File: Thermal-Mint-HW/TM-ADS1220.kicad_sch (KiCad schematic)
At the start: 19 parts, among them U1 ADS1220-VQFN

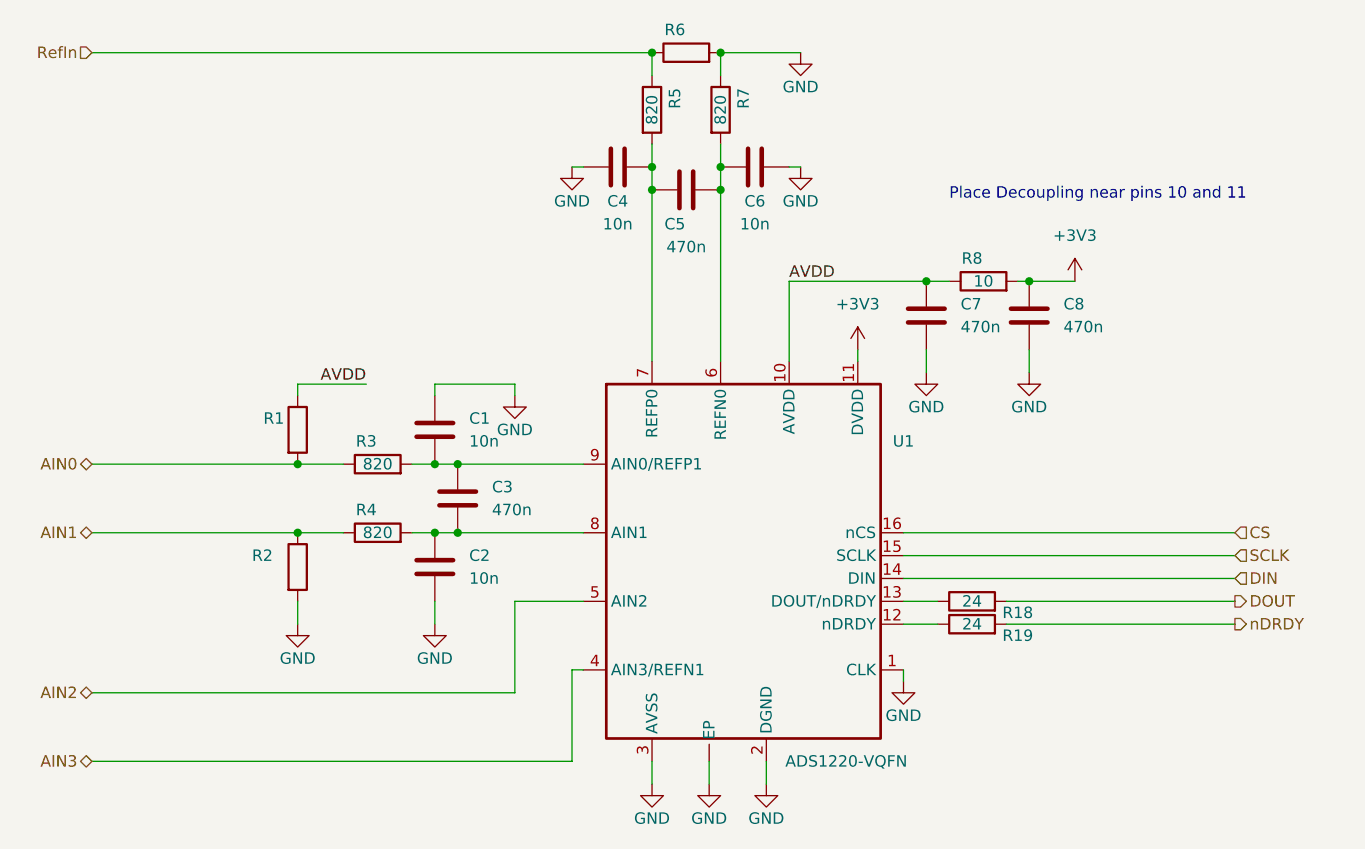
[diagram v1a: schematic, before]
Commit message: Cleanup of Rev1 schematics for review
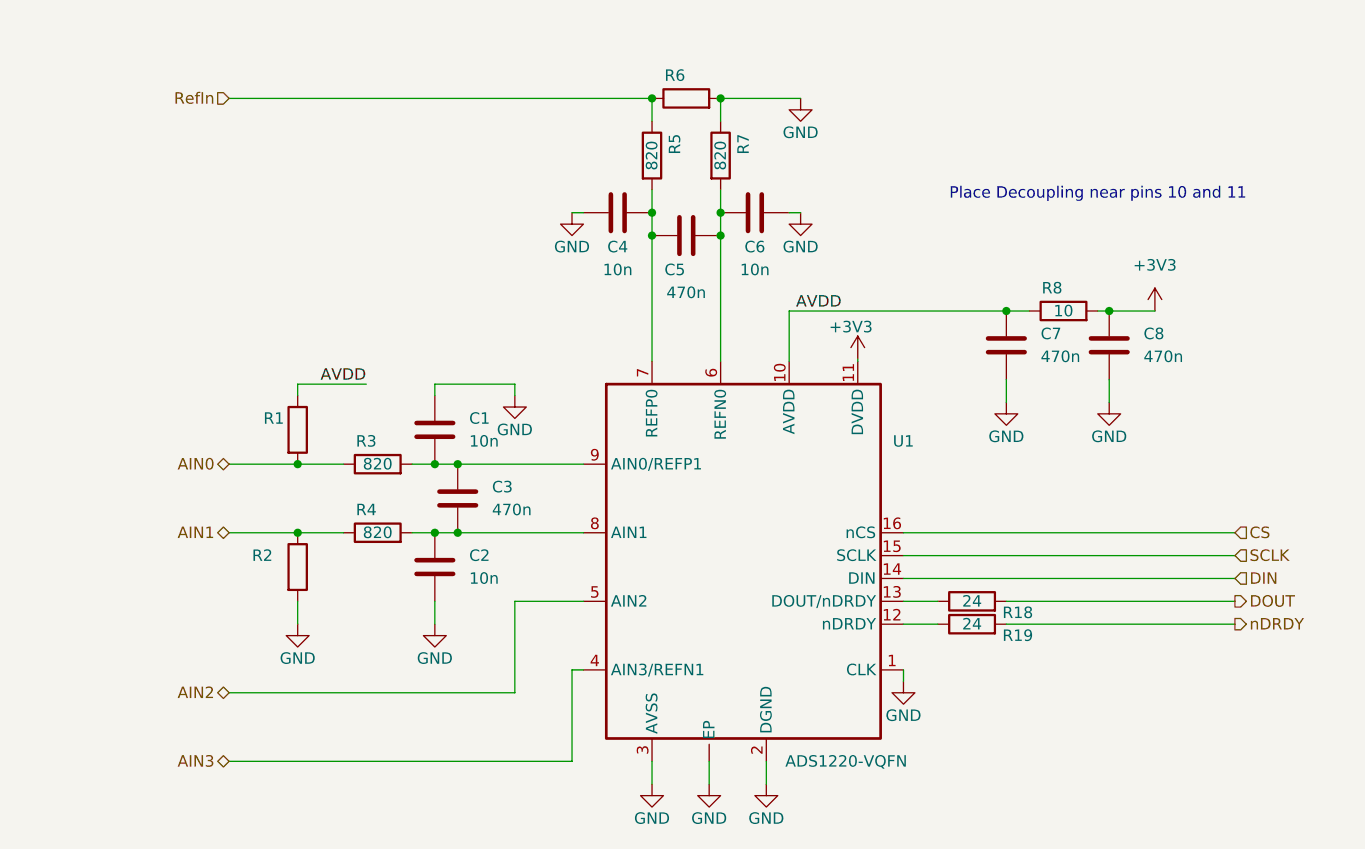
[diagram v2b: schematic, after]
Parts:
- R1, R2: value 10k -> (none); footprint Resistor_SMD:R_0603_1608Metric_Pad0.98x0.95mm_HandSolder -> (none)
- R6: value 1.65k -> (none); footprint Resistor_SMD:R_0603_1608Metric_Pad0.98x0.95mm_HandSolder -> (none)
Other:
- moved on the sheet: C4, C5, C6, C7, C8, R5, R6, R7, R8

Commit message: Temporary commit before changing processor from C3 to s2
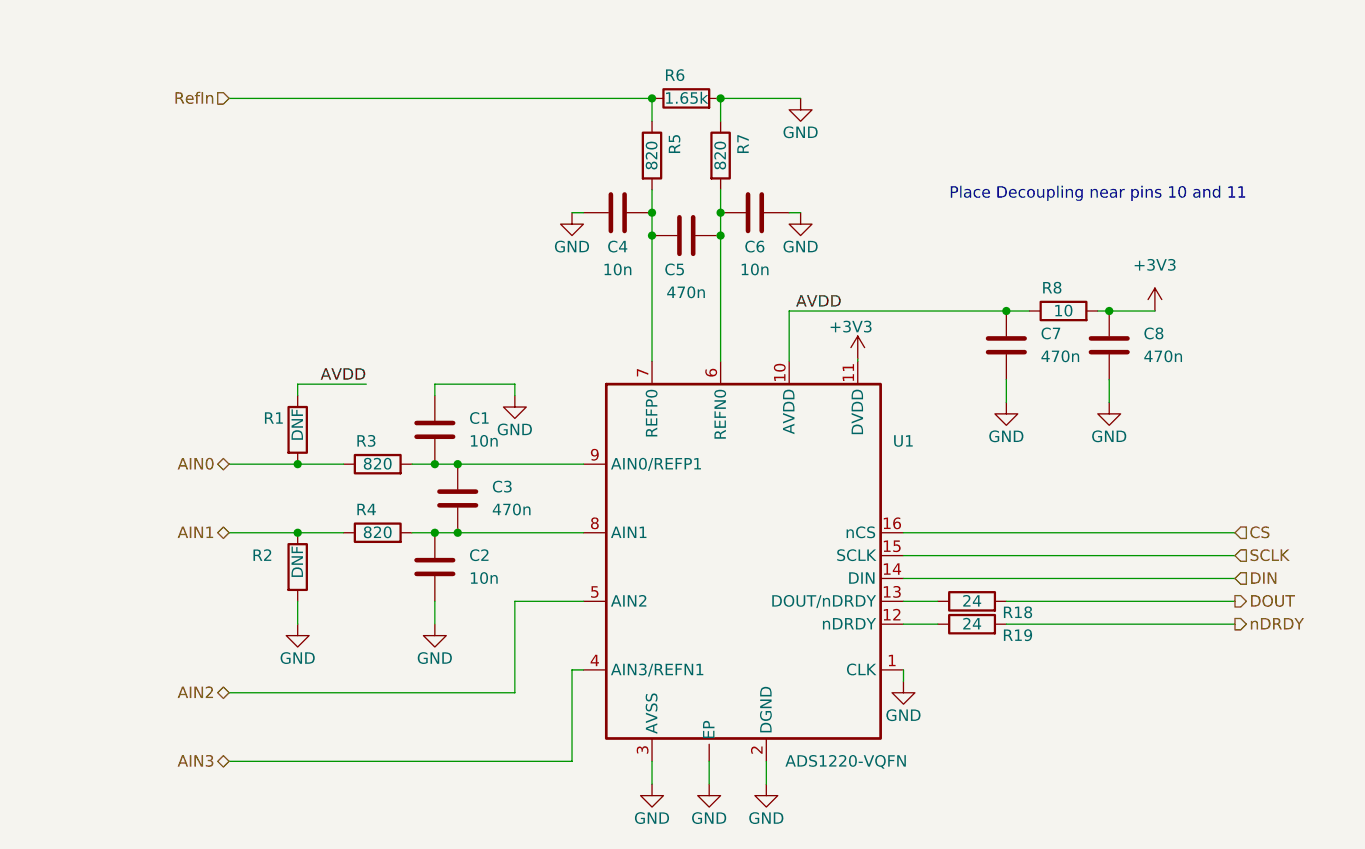
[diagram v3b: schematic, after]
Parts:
- R1, R2: value (none) -> DNF; footprint (none) -> Resistor_SMD:R_0603_1608Metric_Pad0.98x0.95mm_HandSolder
- R6: value (none) -> 1.65k; footprint (none) -> Resistor_SMD:R_0603_1608Metric_Pad0.98x0.95mm_HandSolder

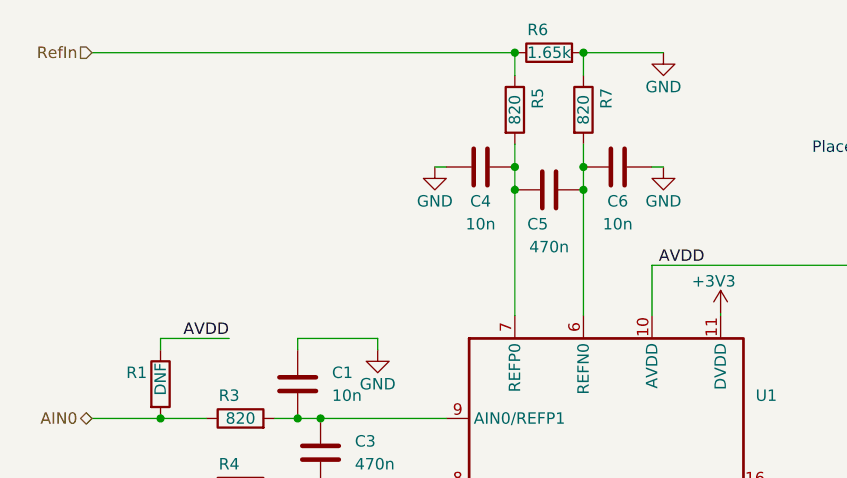
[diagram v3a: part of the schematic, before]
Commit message: Schematic update to ESP32-S2
Updated schematic from ESP32-C3 to the S2 chips with more pins, allowed the removal of the GPO expander and CS mux as well as addition of JTAG
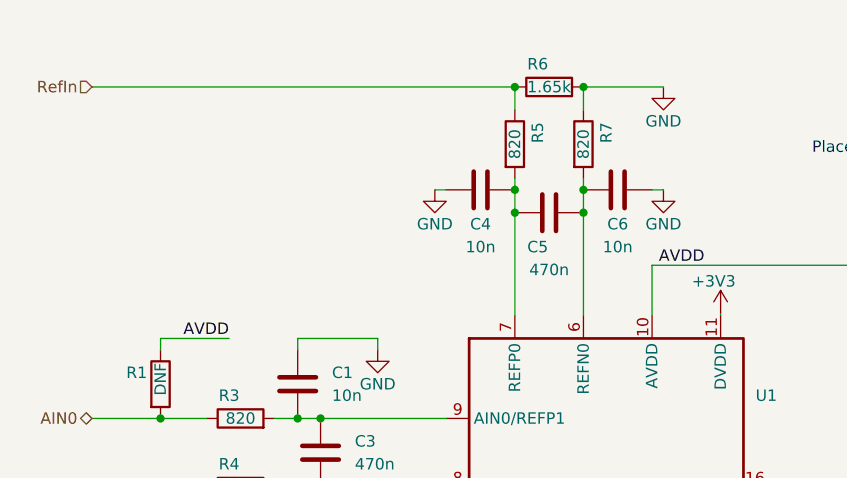
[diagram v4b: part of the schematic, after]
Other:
- moved on the sheet: C4, C5, C6, R5, R6, R7
